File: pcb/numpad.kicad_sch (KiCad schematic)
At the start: 20 parts, among them J2 Molex-505110, J5 JTAG, SW24 Alps SKQG, SW25 Alps SKQG, U1 MDBT50Q-1MV2, Y1 32.768kHz

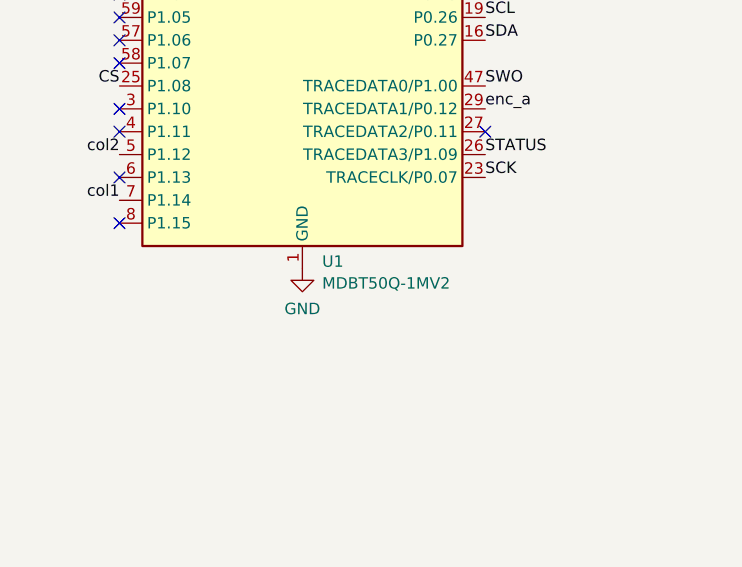
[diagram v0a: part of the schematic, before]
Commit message: Fix BOM and update DRC exclusions
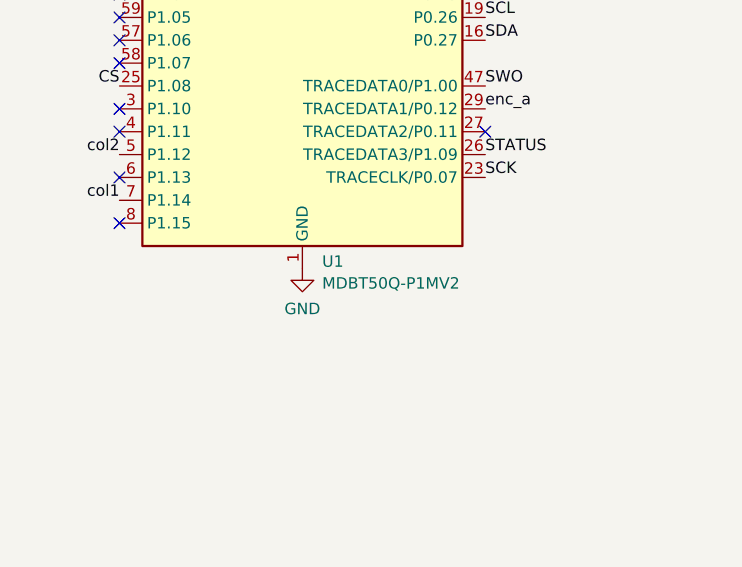
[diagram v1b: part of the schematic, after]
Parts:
- C10, C11: Manufacturer Part Number CC0603GRNPO9BN120 -> CC0402GRNPO9BN120; Package 0603 -> 0402
- U1: value MDBT50Q-1MV2 -> MDBT50Q-P1MV2; Manufacturer Part Number MDBT50Q-1MV2 -> MDBT50Q-P1MV2
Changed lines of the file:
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@@
 			)
 		)
-		(property "Package" "0603"
+		(property "Package" "0402"
 			(at 212.09 63.5 0)
 			(effects
@@
 			)
 		)
-		(property "Manufacturer Part Number" "CC0603GRNPO9BN120"
+		(property "Manufacturer Part Number" "CC0402GRNPO9BN120"
 			(at 212.09 63.5 0)
 			(effects
@@
 			)
 		)
-		(property "Value" "MDBT50Q-1MV2"
-			(at 176.1841 142.5743 0)
+		(property "Value" "MDBT50Q-P1MV2"
+			(at 176.1841 142.5744 0)
 			(effects
 				(font
@@
 			)
 		)
-		(property "Manufacturer Part Number" "MDBT50Q-1MV2"
+		(property "Manufacturer Part Number" "MDBT50Q-P1MV2"
 			(at 173.99 95.25 0)
 			(effects
@@
 			)
 		)
-		(property "Package" "0603"
+		(property "Package" "0402"
 			(at 212.09 58.42 0)
 			(effects
@@
 			)
 		)
-		(property "Manufacturer Part Number" "CC0603GRNPO9BN120"
+		(property "Manufacturer Part Number" "CC0402GRNPO9BN120"
 			(at 212.09 58.42 0)
 			(effects

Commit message: Use switch requiring less force for reset/power
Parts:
- SW25: Manufacturer Part Number SKQGADE010 -> SKQGABE010
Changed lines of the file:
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@@
 			)
 		)
-		(property "Datasheet" "https://tech.alpsalpine.com/e/products/detail/SKQGADE010/"
+		(property "Datasheet" "https://tech.alpsalpine.com/e/products/detail/SKQGABE010/"
 			(at 114.3 135.89 0)
 			(effects
@@
 			)
 		)
-		(property "Manufacturer Part Number" "SKQGADE010"
+		(property "Manufacturer Part Number" "SKQGABE010"
 			(at 114.3 135.89 0)
 			(effects
